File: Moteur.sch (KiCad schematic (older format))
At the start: 52 parts, among them IC1 TPS71501, IC2 TLV710, IC3 MAX3051, IC4 LM5106, IC5 LM5106, IC6 INA282, P1 Bus2, P2 Motor, P3 Bus1, P4 Motor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

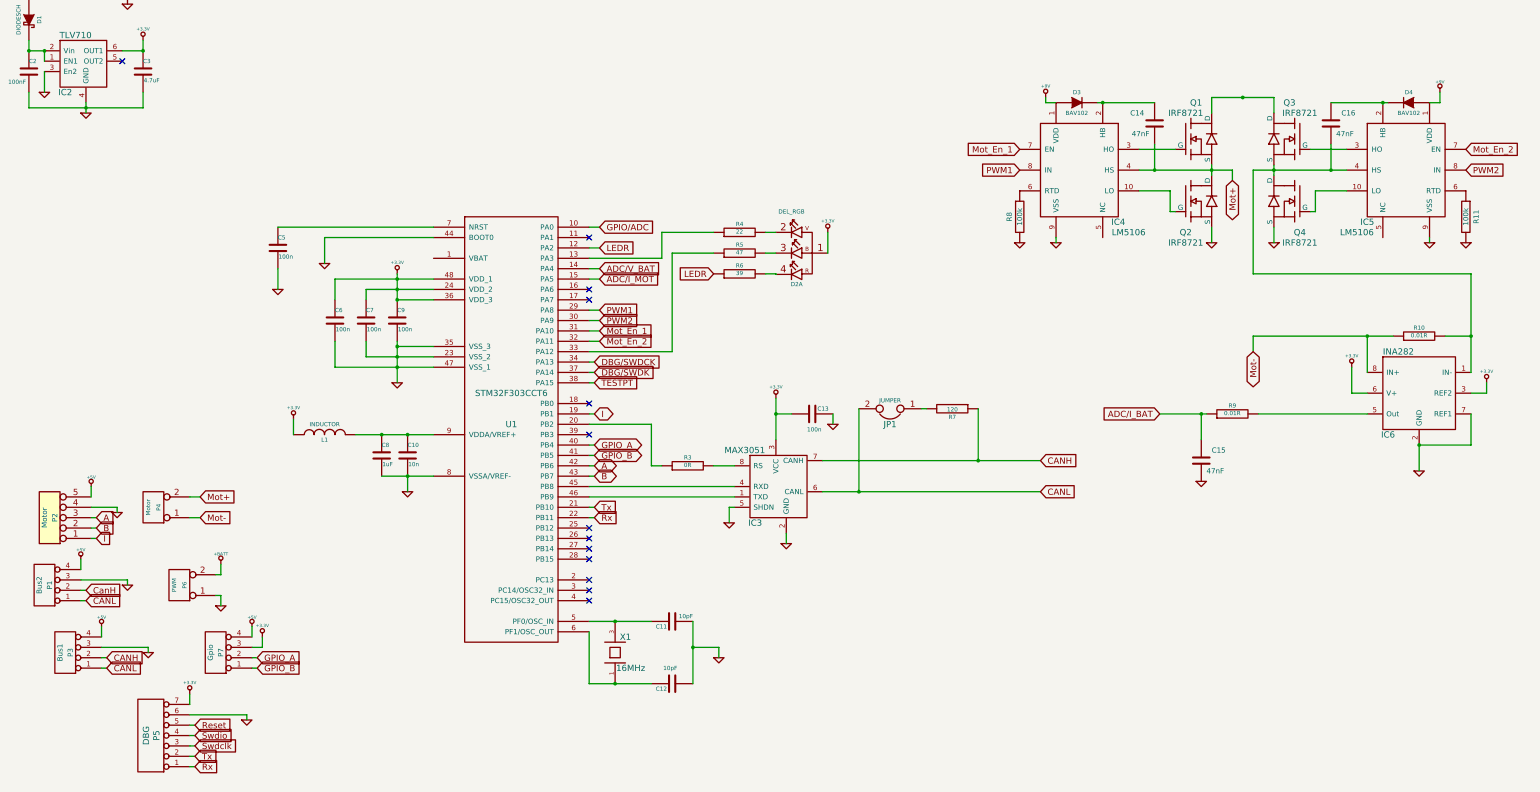
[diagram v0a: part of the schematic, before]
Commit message: minor schematic fixes, start assigning footprints
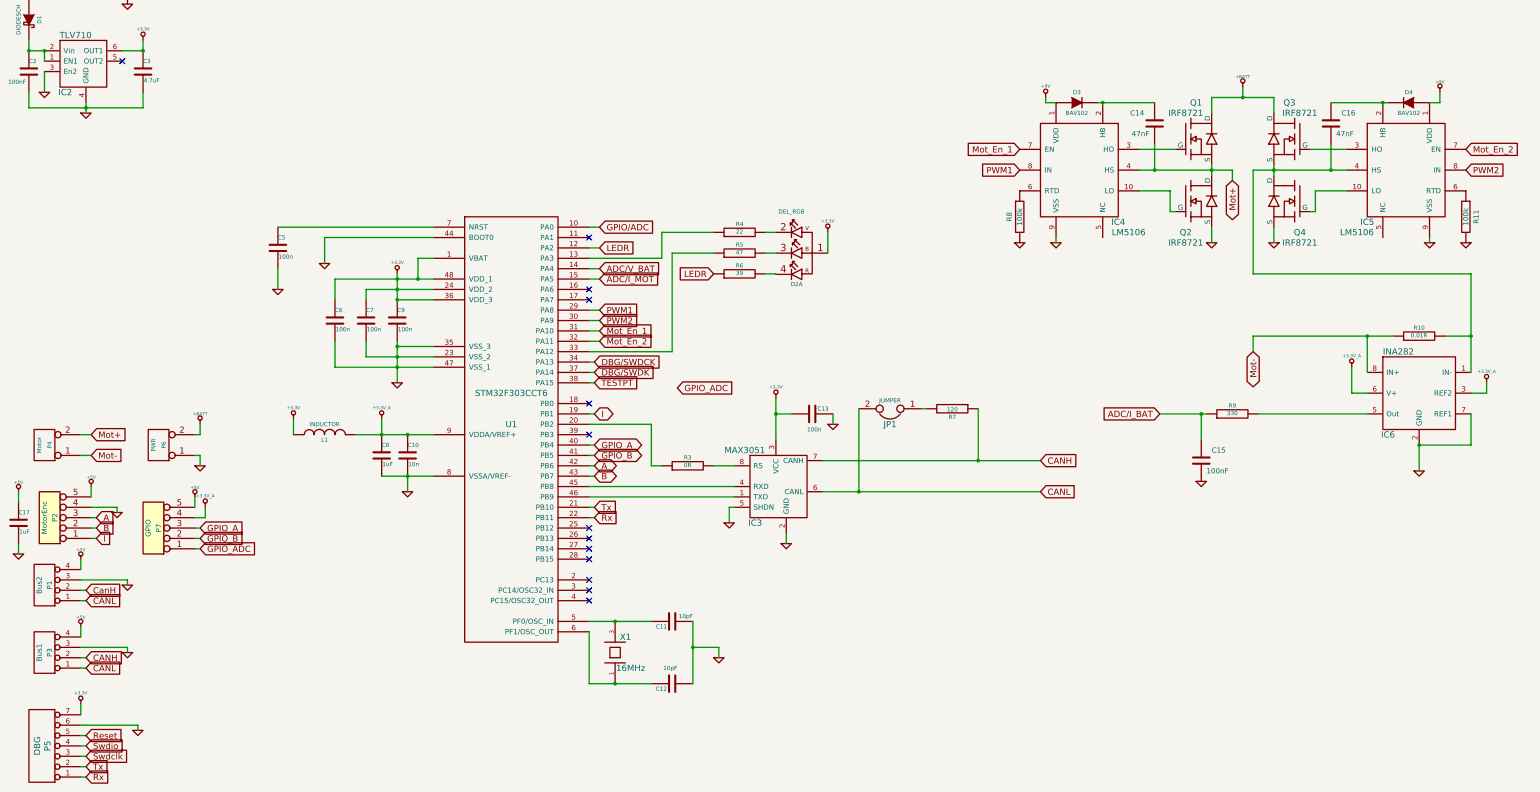
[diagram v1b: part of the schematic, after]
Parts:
- removed P7: Gpio, symbol CONN_4
- added C17: 1uF, ~, symbol C
- added P7: GPIO, ~, symbol CONN_5
- C15: value 47nF -> 100nF
- P2: value Motor -> MotorEnc
- P6: value PWM -> PWR
- R9: value 0.01R -> 330
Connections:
- net +3.3V: now also U1.1 (VBAT); no longer IC6.3 (REF2), IC6.6 (V+)
- net +5V: now also C17.1, P7.5
- net +BATT: now also Q1.5 (D), Q1.6, Q1.7, Q1.8, Q3.5 (D), Q3.6, Q3.7, Q3.8
- net GND: now also C17.2
- net GPIO_A: now also P7.3
- net GPIO_B: now also P7.2
- net +3.3V_A: now reaches C10.1, C8.1, L1.2, U1.9 (VDDA/VREF+)
- net +3.3V_A: now also IC6.3 (REF2), IC6.6 (V+), P7.4
- new net GPIO_ADC: P7.1
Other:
- moved on the sheet: P3, P4, P5, P6

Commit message: connect encoders to diode protected 5V
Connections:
- net labels added: +5V_PROTECTED
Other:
- moved on the sheet: C2
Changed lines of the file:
@@
 L C C2
 U 1 1 5454D868
-P 950 2600
-F 0 "C2" H 950 2700 40  0000 L CNN
-F 1 "100nF" H 750 2500 40  0000 L CNN
-F 2 "~" H 988 2450 30  0000 C CNN
-F 3 "~" H 950 2600 60  0000 C CNN
-	1    950  2600
+P 950 2700
+F 0 "C2" H 950 2800 40  0000 L CNN
+F 1 "100nF" H 750 2600 40  0000 L CNN
+F 2 "~" H 988 2550 30  0000 C CNN
+F 3 "~" H 950 2700 60  0000 C CNN
+	1    950  2700
 	1    0    0    -1
 $EndComp
@@
 Connection ~ 2050 2400
 Wire Wire Line
-	950  2400 1100 2400
+	700  2400 1100 2400
 Connection ~ 950  2400
 Wire Wire Line
@@
 	950  2950 2050 2950
 Wire Wire Line
-	950  2950 950  2800
+	950  2950 950  2900
 Wire Wire Line
 	1500 2900 1500 3000
@@
 	950  1800 950  1900
 Wire Wire Line
-	950  2300 950  2400
+	950  2300 950  2500
 Text GLabel 7550 4550 0    60   Input ~ 0
 LEDR
@@
 	1450 8800 1450 8700
 $Comp
-L +5V #PWR11
-U 1 1 545F878D
-P 1550 6600
-F 0 "#PWR11" H 1550 6690 20  0001 C CNN
-F 1 "+5V" H 1550 6690 30  0000 C CNN
-F 2 "" H 1550 6600 60  0000 C CNN
-F 3 "" H 1550 6600 60  0000 C CNN
-	1    1550 6600
-	1    0    0    -1
-$EndComp
-$Comp
 L +5V #PWR7
 U 1 1 545F8793
@@
 F 3 "" H 1450 7300 60  0000 C CNN
 	1    1450 7300
-	1    0    0    -1
-$EndComp
-$Comp
-L +5V #PWR20
-U 1 1 545F8799
-P 2550 6700
-F 0 "#PWR20" H 2550 6790 20  0001 C CNN
-F 1 "+5V" H 2550 6790 30  0000 C CNN
-F 2 "" H 2550 6700 60  0000 C CNN
-F 3 "" H 2550 6700 60  0000 C CNN
-	1    2550 6700
 	1    0    0    -1
 $EndComp
@@
 	1    0    0    -1
 $EndComp
-$Comp
-L +5V #PWR2
-U 1 1 5464C06E
-P 850 6650
-F 0 "#PWR2" H 850 6740 20  0001 C CNN
-F 1 "+5V" H 850 6740 30  0000 C CNN
-F 2 "" H 850 6650 60  0000 C CNN
-F 3 "" H 850 6650 60  0000 C CNN
-	1    850  6650
-	1    0    0    -1
-$EndComp
 Wire Wire Line
 	850  6750 850  6650
@@
 	1    0    0    -1
 $EndComp
+$Comp
+L +5V_PROTECTED #PWR?
+U 1 1 5464CA8A
+P 700 2400
+F 0 "#PWR?" H 700 2490 20  0001 C CNN
+F 1 "+5V_PROTECTED" H 700 2490 30  0000 C CNN
+F 2 "" H 700 2400 60  0000 C CNN
+F 3 "" H 700 2400 60  0000 C CNN
+	1    700  2400
+	1    0    0    -1
+$EndComp
+$Comp
+L +5V_PROTECTED #PWR?
+U 1 1 5464CB71
+P 1550 6600
+F 0 "#PWR?" H 1550 6690 20  0001 C CNN
+F 1 "+5V_PROTECTED" H 1550 6690 30  0000 C CNN
+F 2 "" H 1550 6600 60  0000 C CNN
+F 3 "" H 1550 6600 60  0000 C CNN
+	1    1550 6600
+	1    0    0    -1
+$EndComp
+$Comp
+L +5V_PROTECTED #PWR?
+U 1 1 5464CB8A
+P 2550 6700
+F 0 "#PWR?" H 2550 6790 20  0001 C CNN
+F 1 "+5V_PROTECTED" H 2550 6790 30  0000 C CNN
+F 2 "" H 2550 6700 60  0000 C CNN
+F 3 "" H 2550 6700 60  0000 C CNN
+	1    2550 6700
+	1    0    0    -1
+$EndComp
+$Comp
+L +5V_PROTECTED #PWR?
+U 1 1 5464CB99
+P 850 6650
+F 0 "#PWR?" H 850 6740 20  0001 C CNN
+F 1 "+5V_PROTECTED" H 850 6740 30  0000 C CNN
+F 2 "" H 850 6650 60  0000 C CNN
+F 3 "" H 850 6650 60  0000 C CNN
+	1    850  6650
+	1    0    0    -1
+$EndComp

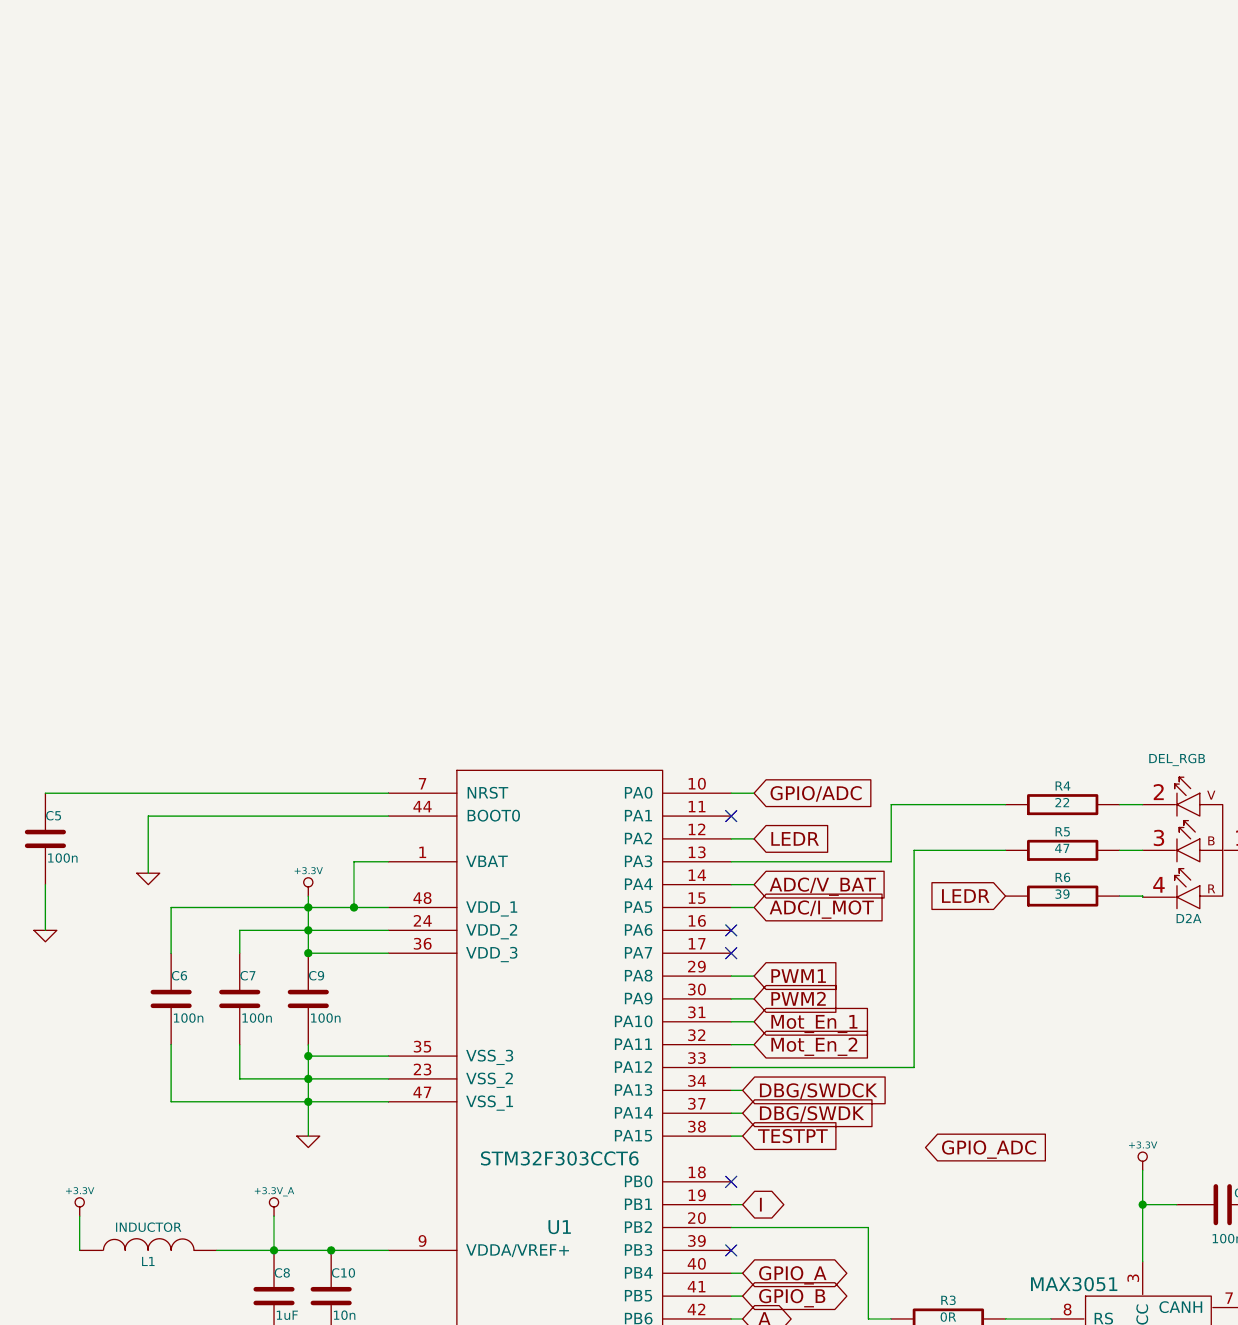
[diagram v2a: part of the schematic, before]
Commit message: add V_Bat resistive divider for ADC
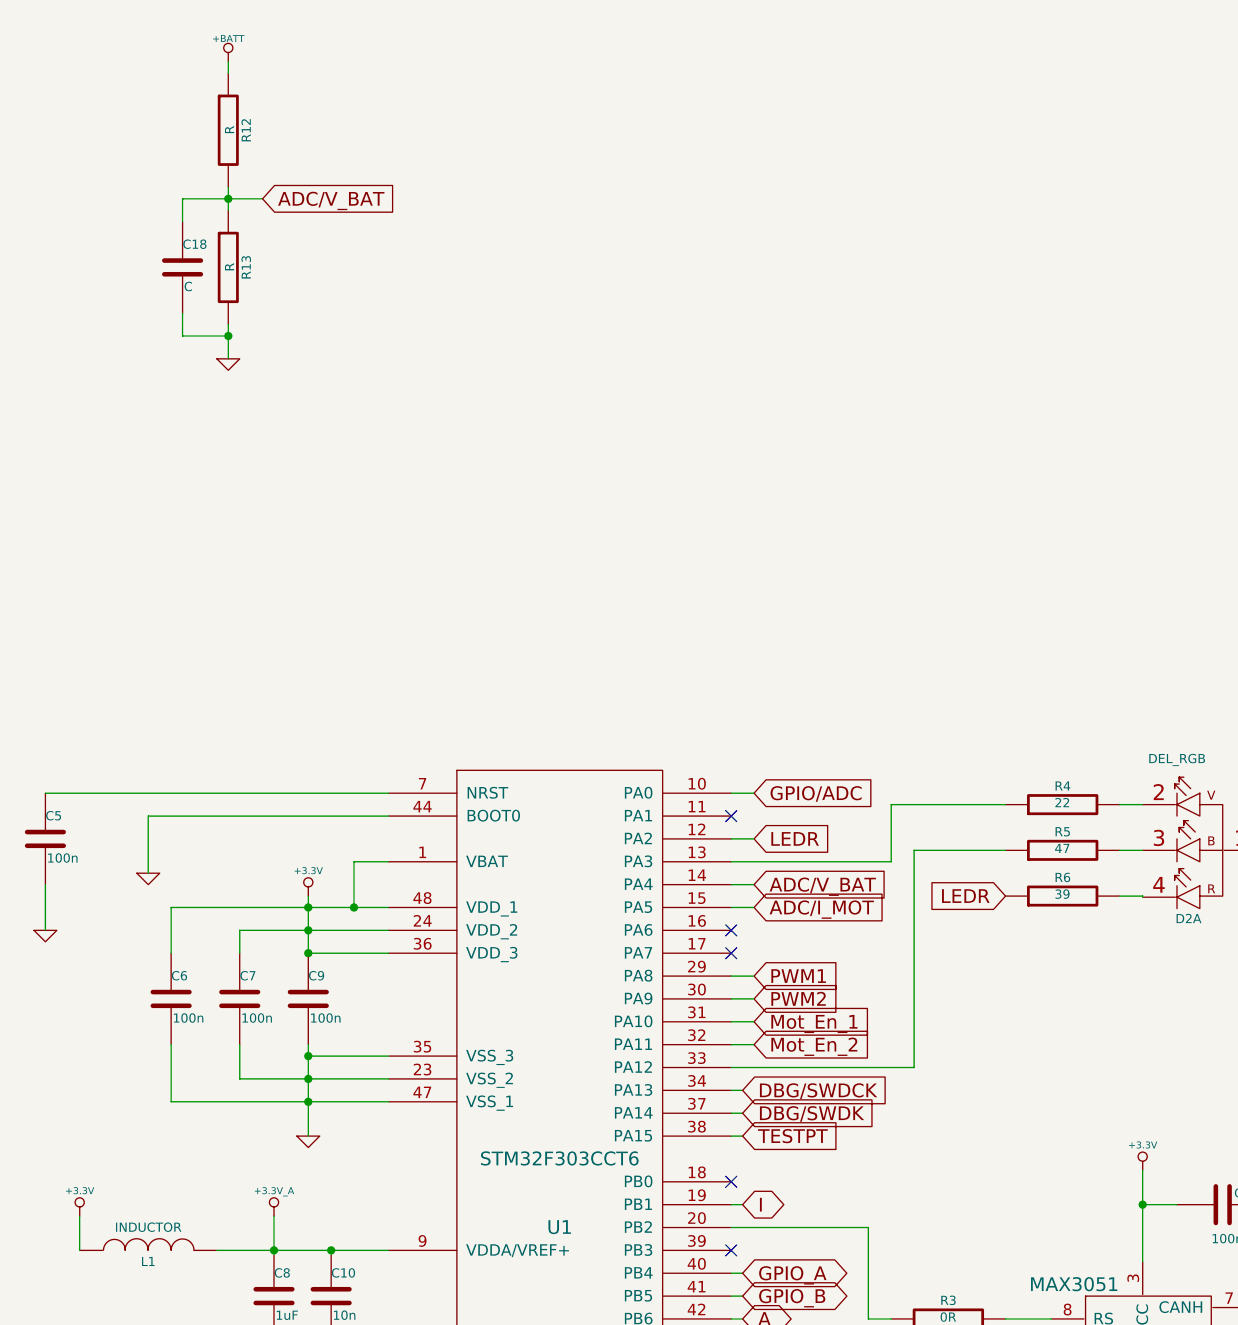
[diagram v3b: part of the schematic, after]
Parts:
- added C18: C, ~, symbol C
- added R12, R13: R, ~, symbol R
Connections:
- wire segments 179 -> 186

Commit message: Fix 5V protected symbol name
Apparently KiCAD has case sensitive symbol names... nice
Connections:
- net labels added: +5V_protected
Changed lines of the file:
@@
 LIBS:_wireless
 LIBS:Moteur-cache
-EELAYER 27 0
+EELAYER 25 0
 EELAYER END
 $Descr A3 16535 11693
@@
 $EndComp
 $Comp
-L +5V_PROTECTED #PWR12
+L +5V_protected #PWR12
 U 1 1 5464CB71
 P 1550 6600
 F 0 "#PWR12" H 1550 6690 20  0001 C CNN
-F 1 "+5V_PROTECTED" H 1550 6690 30  0000 C CNN
+F 1 "+5V_protected" H 1550 6690 30  0000 C CNN
 F 2 "" H 1550 6600 60  0000 C CNN
 F 3 "" H 1550 6600 60  0000 C CNN
@@
 $EndComp
 $Comp
-L +5V_PROTECTED #PWR21
+L +5V_protected #PWR21
 U 1 1 5464CB8A
 P 2550 6700
 F 0 "#PWR21" H 2550 6790 20  0001 C CNN
-F 1 "+5V_PROTECTED" H 2550 6790 30  0000 C CNN
+F 1 "+5V_protected" H 2550 6790 30  0000 C CNN
 F 2 "" H 2550 6700 60  0000 C CNN
 F 3 "" H 2550 6700 60  0000 C CNN
@@
 $EndComp
 $Comp
-L +5V_PROTECTED #PWR3
+L +5V_protected #PWR3
 U 1 1 5464CB99
 P 850 6650
 F 0 "#PWR3" H 850 6740 20  0001 C CNN
-F 1 "+5V_PROTECTED" H 850 6740 30  0000 C CNN
+F 1 "+5V_protected" H 850 6740 30  0000 C CNN
 F 2 "" H 850 6650 60  0000 C CNN
 F 3 "" H 850 6650 60  0000 C CNN

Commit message: Add Diode
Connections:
- wire segments 186 -> 225
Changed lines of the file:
@@
 LIBS:_wireless
 LIBS:Moteur-cache
-EELAYER 25 0
+EELAYER 27 0
 EELAYER END
 $Descr A3 16535 11693
@@
 	12750 3550 12750 4550
 Wire Wire Line
-	12750 3550 13650 3550
+	12750 3550 12950 3550
+Wire Wire Line
+	12950 3550 13500 3550
+Wire Wire Line
+	13500 3550 13650 3550
 Wire Wire Line
 	12950 2850 12950 3000
 Wire Wire Line
-	12350 2850 12950 2850
+	12350 2850 12650 2850
+Wire Wire Line
+	12650 2850 12950 2850
 Connection ~ 11800 3550
 Wire Wire Line
@@
 	11950 3950 12000 3950
 Wire Wire Line
-	12350 3500 12350 3600
+	12350 3500 12350 3550
+Wire Wire Line
+	12350 3550 12350 3600
 Wire Wire Line
 	12350 4100 12350 4250
 Wire Wire Line
-	11250 2900 11800 2900
+	11250 2900 11300 2900
+Wire Wire Line
+	11300 2900 11800 2900
 Connection ~ 11300 2900
 Connection ~ 14000 2900
 Wire Wire Line
-	13500 2900 14050 2900
+	13500 2900 14000 2900
+Wire Wire Line
+	14000 2900 14050 2900
 Wire Wire Line
 	12950 4100 12950 4250
 Wire Wire Line
-	12950 3500 12950 3600
+	12950 3500 12950 3550
+Wire Wire Line
+	12950 3550 12950 3600
 Wire Wire Line
 	13300 3950 13350 3950
@@
 	12350 2850 12350 3000
 Wire Wire Line
-	11650 3550 12550 3550
+	11650 3550 11800 3550
+Wire Wire Line
+	11800 3550 12350 3550
+Wire Wire Line
+	12350 3550 12550 3550
 Wire Wire Line
 	12550 3550 12550 3650
@@
 	14550 2900 14450 2900
 Wire Wire Line
-	1750 950  2250 950
+	1750 950  1900 950
+Wire Wire Line
+	1900 950  2250 950
 Wire Wire Line
 	1750 1100 1750 1450
@@
 Connection ~ 2050 2400
 Wire Wire Line
-	700  2400 1100 2400
+	700  2400 950  2400
+Wire Wire Line
+	950  2400 1100 2400
 Connection ~ 950  2400
 Wire Wire Line
 	2050 2950 2050 2800
 Wire Wire Line
-	950  2950 2050 2950
+	950  2950 1500 2950
+Wire Wire Line
+	1500 2950 2050 2950
 Wire Wire Line
 	950  2950 950  2900
 Wire Wire Line
-	1500 2900 1500 3000
+	1500 2900 1500 2950
+Wire Wire Line
+	1500 2950 1500 3000
 Connection ~ 1500 2950
 Text GLabel 6400 6200 2    60   BiDi ~ 0
@@
 $EndComp
 Wire Wire Line
-	8150 5750 8150 6150
+	8150 5750 8150 5900
+Wire Wire Line
+	8150 5900 8150 6150
 Wire Wire Line
 	8250 7050 8250 7150
@@
 $EndComp
 Wire Wire Line
-	8600 6650 10700 6650
+	8600 6650 8950 6650
+Wire Wire Line
+	8950 6650 10700 6650
 Text GLabel 10700 6350 2    60   Input ~ 0
 CANH
@@
 	6350 8000 6350 8500
 Wire Wire Line
-	6350 7900 6950 7900
-Wire Wire Line
-	6350 8500 6950 8500
+	6350 7900 6600 7900
+Wire Wire Line
+	6600 7900 6950 7900
+Wire Wire Line
+	6350 8500 6600 8500
+Wire Wire Line
+	6600 8500 6950 8500
 $Comp
 L C C11
@@
 Connection ~ 6600 8500
 Wire Wire Line
-	7350 7900 7350 8500
+	7350 7900 7350 8150
+Wire Wire Line
+	7350 8150 7350 8500
 $Comp
 L GND #PWR34
@@
 $EndComp
 Wire Wire Line
-	3900 4600 4850 4600
+	3900 4600 4500 4600
+Wire Wire Line
+	4500 4600 4700 4600
+Wire Wire Line
+	4700 4600 4850 4600
 Wire Wire Line
 	3900 4600 3900 4800
@@
 $EndComp
 Wire Wire Line
-	4200 4700 4850 4700
+	4200 4700 4500 4700
+Wire Wire Line
+	4500 4700 4850 4700
 $Comp
 L C C9
@@
 	4850 5250 4500 5250
 Wire Wire Line
-	4500 5200 4500 5600
-Wire Wire Line
-	4200 5350 4850 5350
+	4500 5200 4500 5250
+Wire Wire Line
+	4500 5250 4500 5350
+Wire Wire Line
+	4500 5350 4500 5450
+Wire Wire Line
+	4500 5450 4500 5600
+Wire Wire Line
+	4200 5350 4500 5350
+Wire Wire Line
+	4500 5350 4850 5350
 Wire Wire Line
 	4200 5350 4200 5200
 Wire Wire Line
-	3900 5450 4850 5450
+	3900 5450 4500 5450
+Wire Wire Line
+	4500 5450 4850 5450
 Wire Wire Line
 	3900 5450 3900 5200
@@
 $EndComp
 Wire Wire Line
-	4500 4550 4500 4800
+	4500 4550 4500 4600
+Wire Wire Line
+	4500 4600 4500 4700
+Wire Wire Line
+	4500 4700 4500 4800
 Connection ~ 4500 4600
 Connection ~ 4500 4700
@@
 $EndComp
 Wire Wire Line
-	4100 6100 4850 6100
-Wire Wire Line
-	4350 6500 4850 6500
+	4100 6100 4350 6100
+Wire Wire Line
+	4350 6100 4600 6100
+Wire Wire Line
+	4600 6100 4850 6100
+Wire Wire Line
+	4350 6500 4600 6500
+Wire Wire Line
+	4600 6500 4850 6500
 $Comp
 L +3.3V #PWR26
@@
 $EndComp
 Wire Wire Line
-	8600 6350 10700 6350
+	8600 6350 10100 6350
+Wire Wire Line
+	10100 6350 10700 6350
 Wire Wire Line
 	8950 5850 8950 6650
@@
 	13850 5900 12800 5900
 Wire Wire Line
-	11850 5900 12300 5900
+	11850 5900 12250 5900
+Wire Wire Line
+	12250 5900 12300 5900
 Wire Wire Line
 	12250 6150 12250 5900
@@
 	950  1800 950  1900
 Wire Wire Line
-	950  2300 950  2500
+	950  2300 950  2400
+Wire Wire Line
+	950  2400 950  2500
 Text GLabel 7550 4550 0    60   Input ~ 0
 LEDR
@@
 LEDR
 Wire Wire Line
-	12750 5150 14100 5150
+	12750 5150 13850 5150
+Wire Wire Line
+	13850 5150 14100 5150
 Wire Wire Line
 	13850 5150 13850 5500
@@
 	14600 5150 14850 5150
 Wire Wire Line
-	14850 4550 14850 5500
+	14850 4550 14850 5150
+Wire Wire Line
+	14850 5150 14850 5500
 Wire Wire Line
 	12750 5150 12750 5300
@@
 	4150 900  4150 950
 Wire Wire Line
-	4150 1450 4150 1550
-Wire Wire Line
-	3950 1500 4300 1500
+	4150 1450 4150 1500
+Wire Wire Line
+	4150 1500 4150 1550
+Wire Wire Line
+	3950 1500 4150 1500
+Wire Wire Line
+	4150 1500 4300 1500
 Wire Wire Line
 	3950 1500 3950 1600
@@
 	3950 2100 4150 2100
 Wire Wire Line
-	4150 2050 4150 2200
+	4150 2050 4150 2100
+Wire Wire Line
+	4150 2100 4150 2200
 $Comp
 L GND #PWR29

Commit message: footprints
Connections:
- wire segments 225 -> 186

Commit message: fix labels, pinout
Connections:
- net labels added: LEDB, LEDG
- net labels removed: CanH, DBG/SWDCK, DBG/SWDK, GPIO/ADC
- wire segments 186 -> 183
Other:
- note added: "Fc = 4.8kHz"
- moved on the sheet: C5, D2A, R4, R5, R6
